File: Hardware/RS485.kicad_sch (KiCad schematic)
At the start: 17 parts

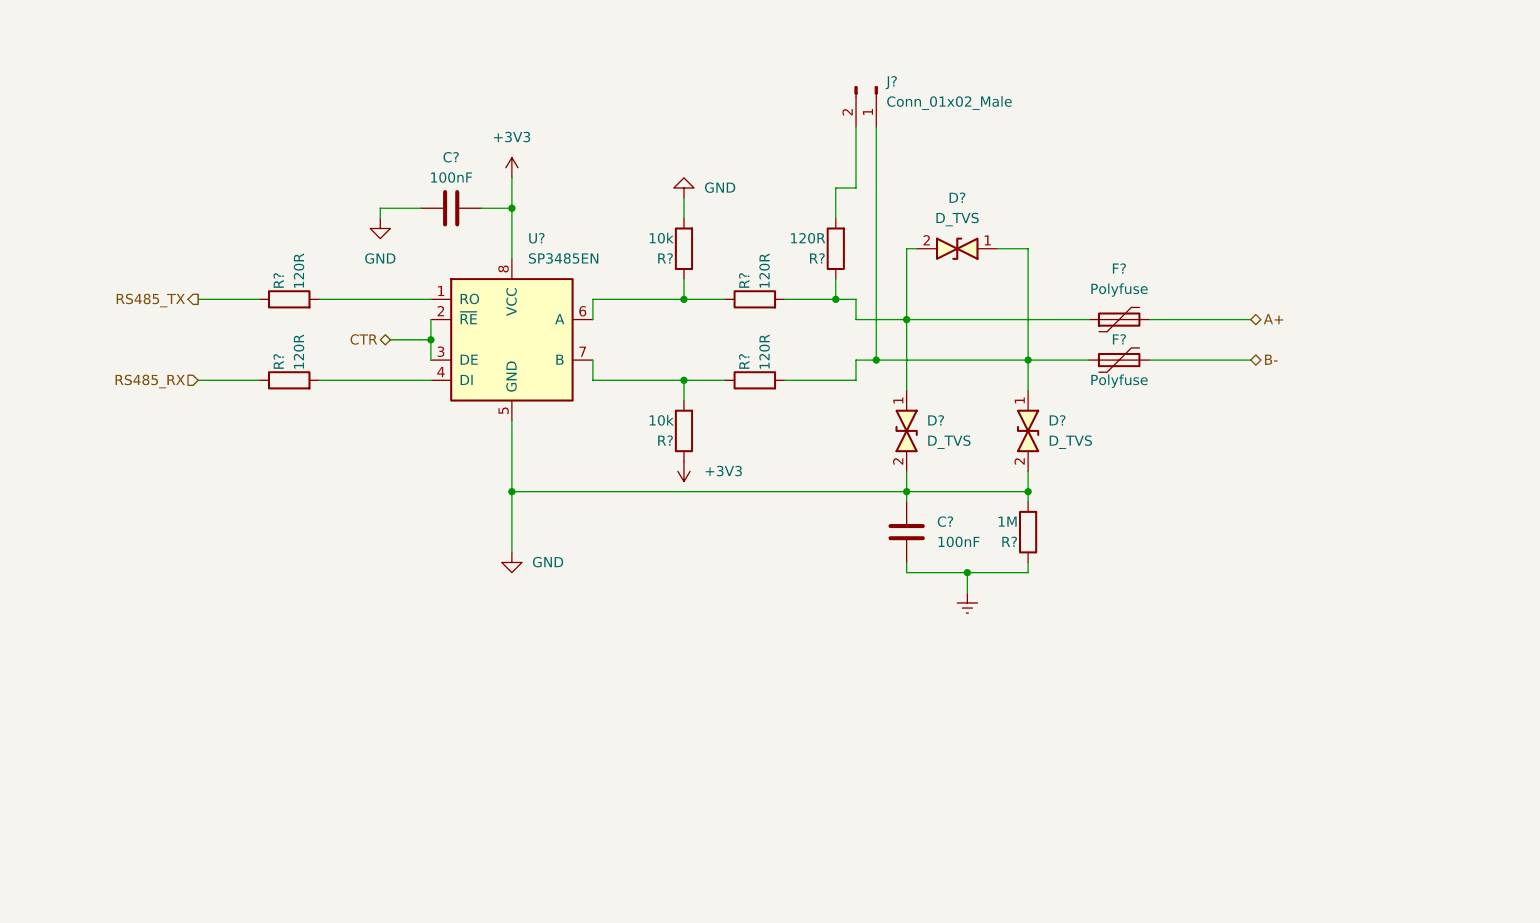
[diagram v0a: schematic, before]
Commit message: remove crytals 32kHz and add Potentiometer in mcp41010
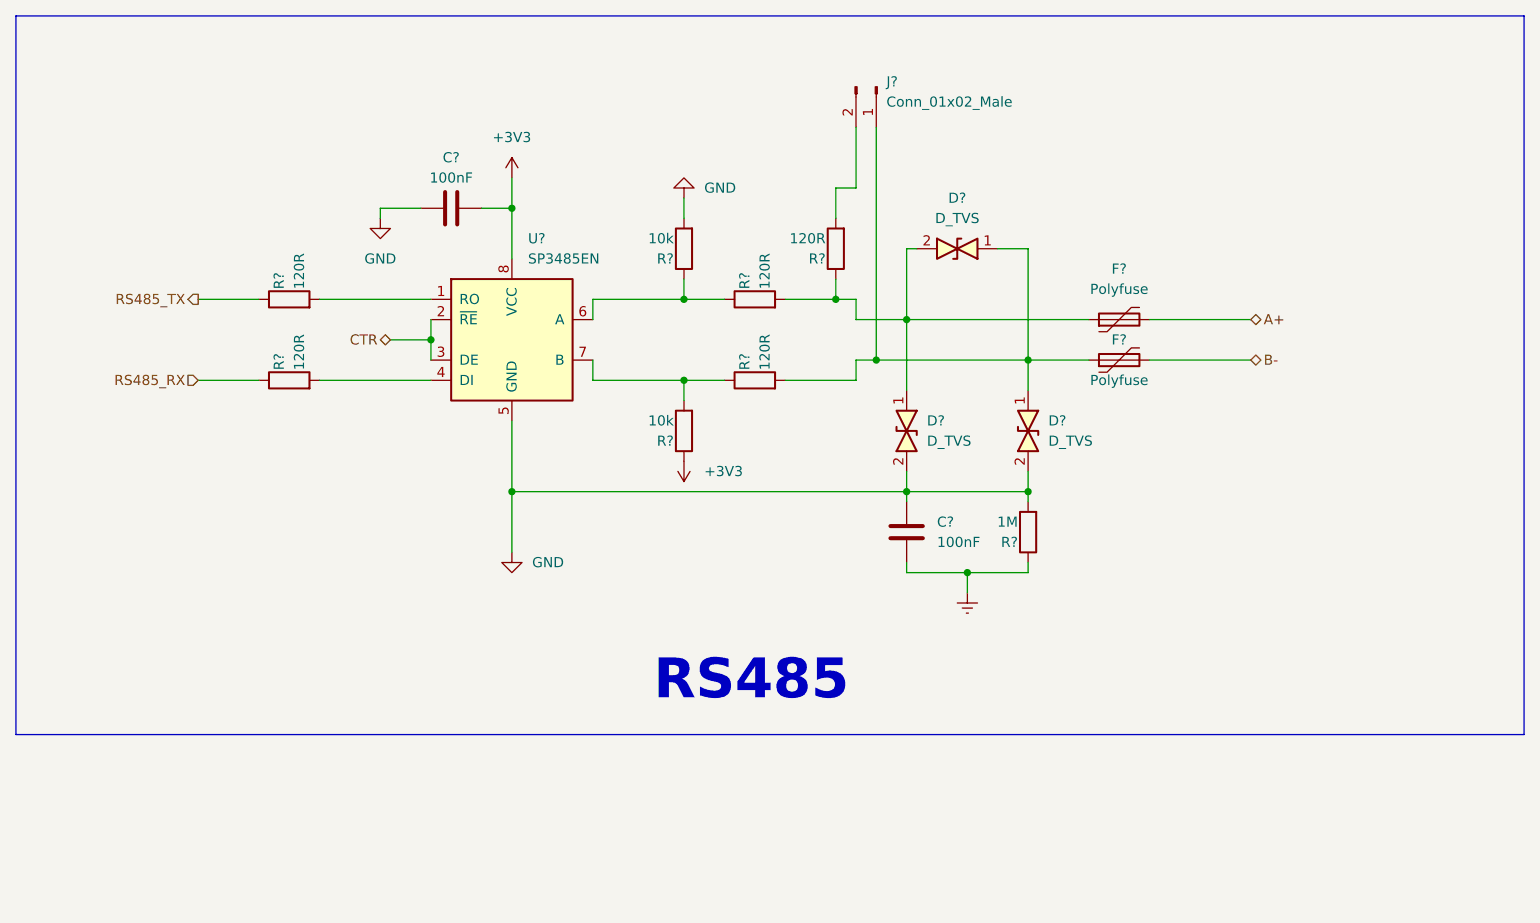
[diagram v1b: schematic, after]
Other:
- note added: "RS485"
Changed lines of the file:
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@@
+    (stroke (width 0) (type default) (color 0 0 0 0))
+  )
+  (polyline (pts (xy 46.99 129.54) (xy 236.22 129.54))
     (stroke (width 0) (type default) (color 0 0 0 0))
   )
@@
   )
   (wire (pts (xy 85.09 74.93) (xy 99.06 74.93))
+    (stroke (width 0) (type default) (color 0 0 0 0))
+  )
+  (polyline (pts (xy 46.99 39.37) (xy 46.99 129.54))
     (stroke (width 0) (type default) (color 0 0 0 0))
   )
@@
   )
   (wire (pts (xy 173.99 82.55) (xy 181.61 82.55))
+    (stroke (width 0) (type default) (color 0 0 0 0))
+  )
+  (polyline (pts (xy 46.99 39.37) (xy 236.22 39.37))
     (stroke (width 0) (type default) (color 0 0 0 0))
   )
@@
     (stroke (width 0) (type default) (color 0 0 0 0))
   )
+  (polyline (pts (xy 236.22 129.54) (xy 236.22 39.37))
+    (stroke (width 0) (type default) (color 0 0 0 0))
+  )
   (wire (pts (xy 130.81 85.09) (xy 135.89 85.09))
     (stroke (width 0) (type default) (color 0 0 0 0))
   )
+  (text "RS485" (at 127 125.73 0)
+    (effects (font (size 5 5) bold) (justify left bottom))
+  )
   (hierarchical_label "A+" (shape bidirectional) (at 201.93 77.47 0)

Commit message: after merge dev
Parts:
- removed R?: 120R, symbol Device:R
- added J20: Screw_Terminal_01x02, symbol Connector:Screw_Terminal_01x02
- added R18: 120R, IVS_FOOTPRINTS:R0603, symbol Device:R
- R19: renamed from R?; footprint (none) -> IVS_FOOTPRINTS:R0603
- gave numbers to parts that had none: 15
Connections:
- net Earth: now also D5.1
- net GND: no longer D5.2
- net at D7.1, F2.1, J2.1 (Pin_1)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: now also D6.2; no longer D6.1
- net at F1.1, R22.2, R24.1: now also D5.2, D6.1; no longer D5.1, D6.2
- net at U8.4 (DI): now also R18.2
- net A+: no longer names the net of F1.2
- net A+: now also J20.1 (Pin_1)
- net B-: no longer names the net of F2.2
- net B-: now also J20.2 (Pin_2)
- net CTR renamed RS485.DERE
- net RS485_TX renamed RS485.TX
- new net RS485.RX: R18.1
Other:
- moved on the sheet: C11, C12, D5, D6, D7, F1, F2, J2, R19, R20, R21, R24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

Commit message: add R0603 footprint
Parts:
- C11: value 100nF -> 1uF; footprint (none) -> IVS_FOOTPRINTS:C0603
- C12: footprint (none) -> IVS_FOOTPRINTS:C0603
- J2: footprint (none) -> Connector_PinHeader_2.54mm:PinHeader_1x02_P2.54mm_Vertical
- R20, R21, R22, R23, R24, R25: footprint (none) -> IVS_FOOTPRINTS:R0603
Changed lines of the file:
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@@
       (effects (font (size 1.27 1.27)) (justify left))
     )
-    (property "Footprint" "" (id 2) (at 139.7 86.868 90)
+    (property "Footprint" "IVS_FOOTPRINTS:R0603" (id 2) (at 139.7 86.868 90)
       (effects (font (size 1.27 1.27)) hide)
     )
@@
     (in_bom yes) (on_board yes) (fields_autoplaced)
     (property "Reference" "C11" (id 0) (at 102.8763 57.15 90))
-    (property "Value" "100nF" (id 1) (at 102.8763 59.69 90))
-    (property "Footprint" "" (id 2) (at 106.68 62.5348 0)
+    (property "Value" "1uF" (id 1) (at 102.8763 59.69 90))
+    (property "Footprint" "IVS_FOOTPRINTS:C0603" (id 2) (at 106.68 62.5348 0)
       (effects (font (size 1.27 1.27)) hide)
     )
@@
       (effects (font (size 1.27 1.27)) (justify left))
     )
-    (property "Footprint" "" (id 2) (at 139.7 76.708 90)
+    (property "Footprint" "IVS_FOOTPRINTS:R0603" (id 2) (at 139.7 76.708 90)
       (effects (font (size 1.27 1.27)) hide)
     )
@@
       (effects (font (size 1.27 1.27)) (justify left))
     )
-    (property "Footprint" "" (id 2) (at 123.952 91.44 90)
+    (property "Footprint" "IVS_FOOTPRINTS:R0603" (id 2) (at 123.952 91.44 90)
       (effects (font (size 1.27 1.27)) hide)
     )
@@
       (effects (font (size 1.27 1.27)) (justify left))
     )
-    (property "Footprint" "" (id 2) (at 169.418 104.14 90)
+    (property "Footprint" "IVS_FOOTPRINTS:R0603" (id 2) (at 169.418 104.14 90)
       (effects (font (size 1.27 1.27)) hide)
     )
@@
       (effects (font (size 1.27 1.27)) (justify right))
     )
-    (property "Footprint" "" (id 2) (at 151.4348 100.33 0)
+    (property "Footprint" "IVS_FOOTPRINTS:C0603" (id 2) (at 151.4348 100.33 0)
       (effects (font (size 1.27 1.27)) hide)
     )
@@
       (effects (font (size 1.27 1.27)) (justify left) hide)
     )
-    (property "Footprint" "" (id 2) (at 154.94 57.15 0)
+    (property "Footprint" "Connector_PinHeader_2.54mm:PinHeader_1x02_P2.54mm_Vertical" (id 2) (at 154.94 57.15 0)
       (effects (font (size 1.27 1.27)) hide)
     )
@@
       (effects (font (size 1.27 1.27)) (justify left))
     )
-    (property "Footprint" "" (id 2) (at 129.032 62.23 90)
+    (property "Footprint" "IVS_FOOTPRINTS:R0603" (id 2) (at 129.032 62.23 90)
       (effects (font (size 1.27 1.27)) hide)
     )
@@
       (effects (font (size 1.27 1.27)) (justify left))
     )
-    (property "Footprint" "" (id 2) (at 154.178 68.58 90)
-      (effects (font (size 1.27 1.27)) hide)
-    )
+    (property "Footprint" "IVS_FOOTPRINTS:R0603" (id 2) (at 154.178 68.58 90)
+      (effects (font (size 1.27 1.27)) hide)
+    )

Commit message: fix pin RS485 tx->rx; rx->tx
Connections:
- net RS485.RX: now also R19.1; no longer R18.1
- net RS485.TX: now also R18.1; no longer R19.1
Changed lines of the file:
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@@
+    (stroke (width 0) (type default) (color 0 0 0 0))
+  )
+  (wire (pts (xy 76.2 85.09) (xy 88.9 85.09))
+    (stroke (width 0) (type default) (color 0 0 0 0))
+  )
+  (wire (pts (xy 76.2 74.93) (xy 89.535 74.93))
     (stroke (width 0) (type default) (color 0 0 0 0))
   )
@@
     (stroke (width 0) (type default) (color 0 0 0 0))
   )
-  (wire (pts (xy 76.2 74.93) (xy 89.535 74.93))
-    (stroke (width 0) (type default) (color 0 0 0 0))
-  )
   (bus (pts (xy 69.85 96.52) (xy 73.66 96.52))
     (stroke (width 0) (type default) (color 0 0 0 0))
@@
   )
   (wire (pts (xy 76.2 99.06) (xy 90.17 99.06))
-    (stroke (width 0) (type default) (color 0 0 0 0))
-  )
-  (wire (pts (xy 76.2 85.09) (xy 88.9 85.09))
     (stroke (width 0) (type default) (color 0 0 0 0))
   )
@@
     (effects (font (size 1.27 1.27)) (justify right bottom))
   )
-  (label "RS485.TX" (at 76.2 74.93 180)
+  (label "RS485.TX" (at 76.2 85.09 180)
     (effects (font (size 1.27 1.27)) (justify right bottom))
   )
-  (label "RS485.RX" (at 76.2 85.09 180)
+  (label "RS485.RX" (at 76.2 74.93 180)
     (effects (font (size 1.27 1.27)) (justify right bottom))
   )

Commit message: fix MCP41010, fix symbol output header
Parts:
- D5, D6, D7: footprint (none) -> IVS_FOOTPRINTS:D_SMA
- F1, F2: footprint (none) -> IVS_FOOTPRINTS:Fuse_1812_4532Metric
- renumbered C11 to C25, C12 to C26, J2 to J4, J20 to J5, R18 to R23, R19 to R24, R20 to R25, R21 to R26, R22 to R27, R23 to R28, R24 to R29, R25 to R30, U8 to U9
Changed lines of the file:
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@@
   (symbol (lib_id "power:GND") (at 96.52 63.5 270) (unit 1)
     (in_bom yes) (on_board yes) (fields_autoplaced)
-    (property "Reference" "#PWR0149" (id 0) (at 90.17 63.5 0)
+    (property "Reference" "#PWR058" (id 0) (at 90.17 63.5 0)
       (effects (font (size 1.27 1.27)) hide)
     )
@@
   (symbol (lib_id "Device:R") (at 139.7 85.09 90) (unit 1)
     (in_bom yes) (on_board yes)
-    (property "Reference" "R23" (id 0) (at 138.43 83.82 0)
+    (property "Reference" "R28" (id 0) (at 138.43 83.82 0)
       (effects (font (size 1.27 1.27)) (justify left))
     )
@@
   (symbol (lib_id "Device:C") (at 102.87 63.5 90) (unit 1)
     (in_bom yes) (on_board yes) (fields_autoplaced)
-    (property "Reference" "C11" (id 0) (at 102.8763 57.15 90))
+    (property "Reference" "C25" (id 0) (at 102.8763 57.15 90))
     (property "Value" "1uF" (id 1) (at 102.8763 59.69 90))
     (property "Footprint" "IVS_FOOTPRINTS:C0603" (id 2) (at 106.68 62.5348 0)
@@
   (symbol (lib_id "Device:R") (at 139.7 74.93 90) (unit 1)
     (in_bom yes) (on_board yes)
-    (property "Reference" "R22" (id 0) (at 138.43 73.66 0)
+    (property "Reference" "R27" (id 0) (at 138.43 73.66 0)
       (effects (font (size 1.27 1.27)) (justify left))
     )
@@
       (effects (font (size 1.27 1.27)) (justify right))
     )
-    (property "Footprint" "" (id 2) (at 167.64 91.44 0)
+    (property "Footprint" "IVS_FOOTPRINTS:D_SMA" (id 2) (at 167.64 91.44 0)
       (effects (font (size 1.27 1.27)) hide)
     )
@@
   (symbol (lib_id "power:+3V3") (at 109.22 59.69 0) (unit 1)
     (in_bom yes) (on_board yes) (fields_autoplaced)
-    (property "Reference" "#PWR0152" (id 0) (at 109.22 63.5 0)
+    (property "Reference" "#PWR059" (id 0) (at 109.22 63.5 0)
       (effects (font (size 1.27 1.27)) hide)
     )
@@
   (symbol (lib_id "power:GND") (at 109.22 106.68 0) (unit 1)
     (in_bom yes) (on_board yes) (fields_autoplaced)
-    (property "Reference" "#PWR0150" (id 0) (at 109.22 113.03 0)
+    (property "Reference" "#PWR060" (id 0) (at 109.22 113.03 0)
       (effects (font (size 1.27 1.27)) hide)
     )
@@
   (symbol (lib_id "Device:R") (at 125.73 91.44 0) (unit 1)
     (in_bom yes) (on_board yes)
-    (property "Reference" "R20" (id 0) (at 127 90.17 0)
+    (property "Reference" "R25" (id 0) (at 127 90.17 0)
       (effects (font (size 1.27 1.27)) (justify left))
     )
@@
       (effects (font (size 1.27 1.27)) (justify right))
     )
-    (property "Footprint" "" (id 2) (at 167.64 80.01 0)
+    (property "Footprint" "IVS_FOOTPRINTS:D_SMA" (id 2) (at 167.64 80.01 0)
       (effects (font (size 1.27 1.27)) hide)
     )
@@
   (symbol (lib_id "Device:R") (at 167.64 104.14 180) (unit 1)
     (in_bom yes) (on_board yes)
-    (property "Reference" "R25" (id 0) (at 166.37 105.41 0)
+    (property "Reference" "R30" (id 0) (at 166.37 105.41 0)
       (effects (font (size 1.27 1.27)) (justify left))
     )
@@
   (symbol (lib_id "Device:C") (at 152.4 104.14 180) (unit 1)
     (in_bom yes) (on_board yes) (fields_autoplaced)
-    (property "Reference" "C12" (id 0) (at 156.21 102.8699 0)
+    (property "Reference" "C26" (id 0) (at 156.21 102.8699 0)
       (effects (font (size 1.27 1.27)) (justify right))
     )
@@
   (symbol (lib_id "Connector:Conn_01x02_Male") (at 154.94 57.15 270) (unit 1)
     (in_bom yes) (on_board yes)
-    (property "Reference" "J2" (id 0) (at 156.21 56.5149 90)
+    (property "Reference" "J4" (id 0) (at 156.21 56.5149 90)
       (effects (font (size 1.27 1.27)) (justify left))
     )
@@
   (symbol (lib_id "Device:R") (at 92.71 85.09 90) (unit 1)
     (in_bom yes) (on_board yes)
-    (property "Reference" "R18" (id 0) (at 88.9 83.82 90)
+    (property "Reference" "R23" (id 0) (at 88.9 83.82 90)
       (effects (font (size 1.27 1.27)) (justify left))
     )
@@
   (symbol (lib_id "power:Earth") (at 167.64 62.23 180) (unit 1)
     (in_bom yes) (on_board yes) (fields_autoplaced)
-    (property "Reference" "#PWR0142" (id 0) (at 167.64 55.88 0)
+    (property "Reference" "#PWR063" (id 0) (at 167.64 55.88 0)
       (effects (font (size 1.27 1.27)) hide)
     )
@@
     (property "Reference" "F2" (id 0) (at 185.42 82.55 90))
     (property "Value" "Polyfuse" (id 1) (at 185.42 87.63 90))
-    (property "Footprint" "" (id 2) (at 190.5 83.82 0)
+    (property "Footprint" "IVS_FOOTPRINTS:Fuse_1812_4532Metric" (id 2) (at 190.5 83.82 0)
       (effects (font (size 1.27 1.27)) (justify left) hide)
     )
@@
   (symbol (lib_id "power:Earth") (at 160.02 111.76 0) (unit 1)
     (in_bom yes) (on_board yes) (fields_autoplaced)
-    (property "Reference" "#PWR0151" (id 0) (at 160.02 118.11 0)
+    (property "Reference" "#PWR062" (id 0) (at 160.02 118.11 0)
       (effects (font (size 1.27 1.27)) hide)
     )
@@
   (symbol (lib_id "Connector:Screw_Terminal_01x02") (at 208.28 78.74 0) (unit 1)
     (in_bom yes) (on_board yes) (fields_autoplaced)
-    (property "Reference" "J20" (id 0) (at 210.82 78.7399 0)
+    (property "Reference" "J5" (id 0) (at 210.82 78.7399 0)
       (effects (font (size 1.27 1.27)) (justify left))
     )
@@
     (property "Reference" "F1" (id 0) (at 185.42 68.58 90))
     (property "Value" "Polyfuse" (id 1) (at 185.42 71.12 90))
-    (property "Footprint" "" (id 2) (at 190.5 73.66 0)
+    (property "Footprint" "IVS_FOOTPRINTS:Fuse_1812_4532Metric" (id 2) (at 190.5 73.66 0)
       (effects (font (size 1.27 1.27)) (justify left) hide)
     )
@@
   (symbol (lib_id "Device:R") (at 93.345 74.93 90) (unit 1)
     (in_bom yes) (on_board yes)
-    (property "Reference" "R19" (id 0) (at 90.17 73.66 90)
+    (property "Reference" "R24" (id 0) (at 90.17 73.66 90)
       (effects (font (size 1.27 1.27)) (justify left))
     )
@@
       (effects (font (size 1.27 1.27)) (justify right))
     )
-    (property "Footprint" "" (id 2) (at 167.64 68.58 0)
+    (property "Footprint" "IVS_FOOTPRINTS:D_SMA" (id 2) (at 167.64 68.58 0)
       (effects (font (size 1.27 1.27)) hide)
     )
@@
   (symbol (lib_id "Device:R") (at 130.81 62.23 0) (unit 1)
     (in_bom yes) (on_board yes)
-    (property "Reference" "R21" (id 0) (at 132.08 60.96 0)
+    (property "Reference" "R26" (id 0) (at 132.08 60.96 0)
       (effects (font (size 1.27 1.27)) (justify left))
     )
@@
   (symbol (lib_id "power:+3V3") (at 130.81 58.42 0) (unit 1)
     (in_bom yes) (on_board yes) (fields_autoplaced)
-    (property "Reference" "#PWR0154" (id 0) (at 130.81 62.23 0)
+    (property "Reference" "#PWR061" (id 0) (at 130.81 62.23 0)
       (effects (font (size 1.27 1.27)) hide)
     )
@@
   (symbol (lib_id "Device:R") (at 152.4 68.58 180) (unit 1)
     (in_bom yes) (on_board yes)
-    (property "Reference" "R24" (id 0) (at 151.13 69.85 0)
+    (property "Reference" "R29" (id 0) (at 151.13 69.85 0)
       (effects (font (size 1.27 1.27)) (justify left))
     )
@@
   (symbol (lib_id "Interface_UART:SP3485EN") (at 109.22 80.01 0) (unit 1)
     (in_bom yes) (on_board yes) (fields_autoplaced)
-    (property "Reference" "U8" (id 0) (at 111.2394 67.31 0)
-      (effects (font (size 1.27 1.27)) (justify left))
-    )
+    (property "Reference" "U9" (id 0) (at 111.2394 67.31 0)
+      (effects (font (size 1.27 1.27)) (justify left))
+    )

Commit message: add footprint
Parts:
- J5: footprint (none) -> IVS_FOOTPRINTS:HT-3.96mm-2Pin
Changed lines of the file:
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@@
       (effects (font (size 1.27 1.27)) (justify left) hide)
     )
-    (property "Footprint" "" (id 2) (at 208.28 78.74 0)
+    (property "Footprint" "IVS_FOOTPRINTS:HT-3.96mm-2Pin" (id 2) (at 208.28 78.74 0)
       (effects (font (size 1.27 1.27)) hide)
     )

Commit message: add all footprint
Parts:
- renumbered J4 to J5, J5 to J6
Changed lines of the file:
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@@
   (symbol (lib_id "power:GND") (at 96.52 63.5 270) (unit 1)
     (in_bom yes) (on_board yes) (fields_autoplaced)
-    (property "Reference" "#PWR058" (id 0) (at 90.17 63.5 0)
+    (property "Reference" "#PWR061" (id 0) (at 90.17 63.5 0)
       (effects (font (size 1.27 1.27)) hide)
     )
@@
   (symbol (lib_id "power:+3V3") (at 109.22 59.69 0) (unit 1)
     (in_bom yes) (on_board yes) (fields_autoplaced)
-    (property "Reference" "#PWR059" (id 0) (at 109.22 63.5 0)
+    (property "Reference" "#PWR062" (id 0) (at 109.22 63.5 0)
       (effects (font (size 1.27 1.27)) hide)
     )
@@
   (symbol (lib_id "power:GND") (at 109.22 106.68 0) (unit 1)
     (in_bom yes) (on_board yes) (fields_autoplaced)
-    (property "Reference" "#PWR060" (id 0) (at 109.22 113.03 0)
+    (property "Reference" "#PWR063" (id 0) (at 109.22 113.03 0)
       (effects (font (size 1.27 1.27)) hide)
     )
@@
   (symbol (lib_id "Connector:Conn_01x02_Male") (at 154.94 57.15 270) (unit 1)
     (in_bom yes) (on_board yes)
-    (property "Reference" "J4" (id 0) (at 156.21 56.5149 90)
+    (property "Reference" "J5" (id 0) (at 156.21 56.5149 90)
       (effects (font (size 1.27 1.27)) (justify left))
     )
@@
   (symbol (lib_id "power:Earth") (at 167.64 62.23 180) (unit 1)
     (in_bom yes) (on_board yes) (fields_autoplaced)
-    (property "Reference" "#PWR063" (id 0) (at 167.64 55.88 0)
+    (property "Reference" "#PWR066" (id 0) (at 167.64 55.88 0)
       (effects (font (size 1.27 1.27)) hide)
     )
@@
   (symbol (lib_id "power:Earth") (at 160.02 111.76 0) (unit 1)
     (in_bom yes) (on_board yes) (fields_autoplaced)
-    (property "Reference" "#PWR062" (id 0) (at 160.02 118.11 0)
+    (property "Reference" "#PWR065" (id 0) (at 160.02 118.11 0)
       (effects (font (size 1.27 1.27)) hide)
     )
@@
   (symbol (lib_id "Connector:Screw_Terminal_01x02") (at 208.28 78.74 0) (unit 1)
     (in_bom yes) (on_board yes) (fields_autoplaced)
-    (property "Reference" "J5" (id 0) (at 210.82 78.7399 0)
+    (property "Reference" "J6" (id 0) (at 210.82 78.7399 0)
       (effects (font (size 1.27 1.27)) (justify left))
     )
@@
   (symbol (lib_id "power:+3V3") (at 130.81 58.42 0) (unit 1)
     (in_bom yes) (on_board yes) (fields_autoplaced)
-    (property "Reference" "#PWR061" (id 0) (at 130.81 62.23 0)
-      (effects (font (size 1.27 1.27)) hide)
-    )
+    (property "Reference" "#PWR064" (id 0) (at 130.81 62.23 0)
+      (effects (font (size 1.27 1.27)) hide)
+    )
